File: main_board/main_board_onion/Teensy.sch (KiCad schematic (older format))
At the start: 6 parts, among them Q6 BSS138, Q7 2N7002E, U8 Teensy-LC

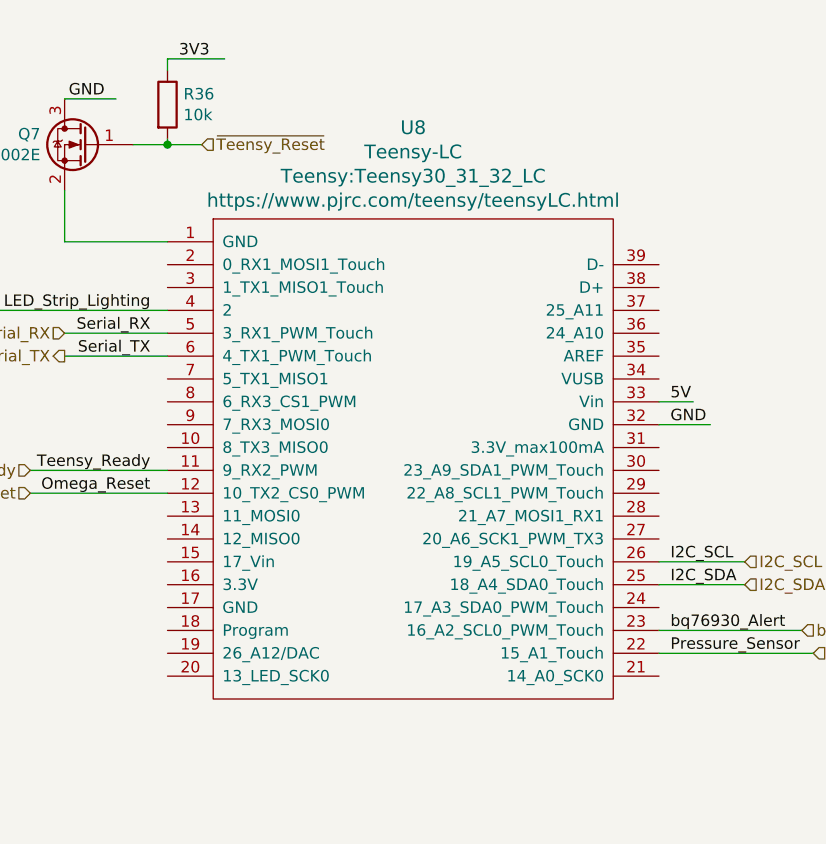
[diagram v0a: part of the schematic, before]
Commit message: Added nRF page and Adafruit Trinket files
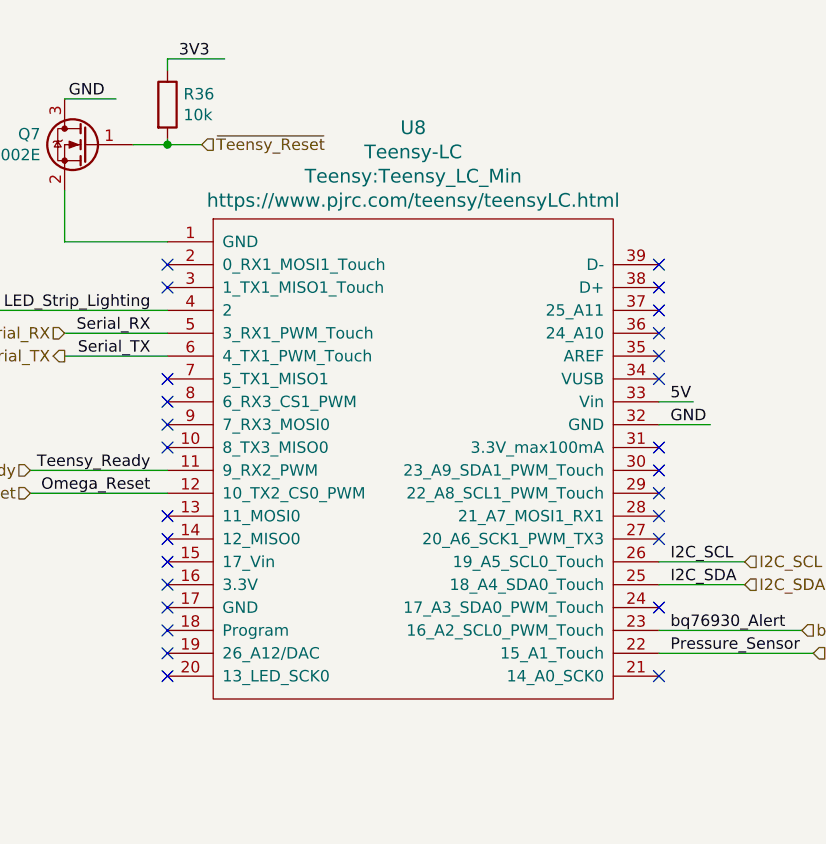
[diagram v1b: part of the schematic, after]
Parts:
- U8: footprint Teensy:Teensy30_31_32_LC -> Teensy:Teensy_LC_Min
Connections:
- no-connect marks 0 -> 27
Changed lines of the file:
@@
 $Descr A4 11693 8268
 encoding utf-8
-Sheet 5 5
+Sheet 5 6
 Title ""
 Date ""
@@
 F 0 "U8" H 5775 4874 60  0000 C CNN
 F 1 "Teensy-LC" H 5775 4768 60  0000 C CNN
-F 2 "Teensy:Teensy30_31_32_LC" H 5775 4662 60  0000 C CNN
+F 2 "Teensy:Teensy_LC_Min" H 5775 4662 60  0000 C CNN
 F 3 "https://www.pjrc.com/teensy/teensyLC.html" H 5775 4556 60  0000 C CNN
 	1    5750 3425
@@
 Text HLabel 4850 2050 2    50   Input ~ 0
 ~Teensy_Reset
+NoConn ~ 6850 2575
+NoConn ~ 6850 2675
+NoConn ~ 6850 2775
+NoConn ~ 6850 2875
+NoConn ~ 6850 2975
+NoConn ~ 6850 3075
+NoConn ~ 6850 3375
+NoConn ~ 6850 3475
+NoConn ~ 6850 3575
+NoConn ~ 6850 3675
+NoConn ~ 6850 3775
+NoConn ~ 6850 4075
+NoConn ~ 6850 4375
+NoConn ~ 4700 4375
+NoConn ~ 4700 4275
+NoConn ~ 4700 4175
+NoConn ~ 4700 4075
+NoConn ~ 4700 3975
+NoConn ~ 4700 3875
+NoConn ~ 4700 3775
+NoConn ~ 4700 3675
+NoConn ~ 4700 3375
+NoConn ~ 4700 3275
+NoConn ~ 4700 3175
+NoConn ~ 4700 3075
+NoConn ~ 4700 2675
+NoConn ~ 4700 2575
 $EndSCHEMATC

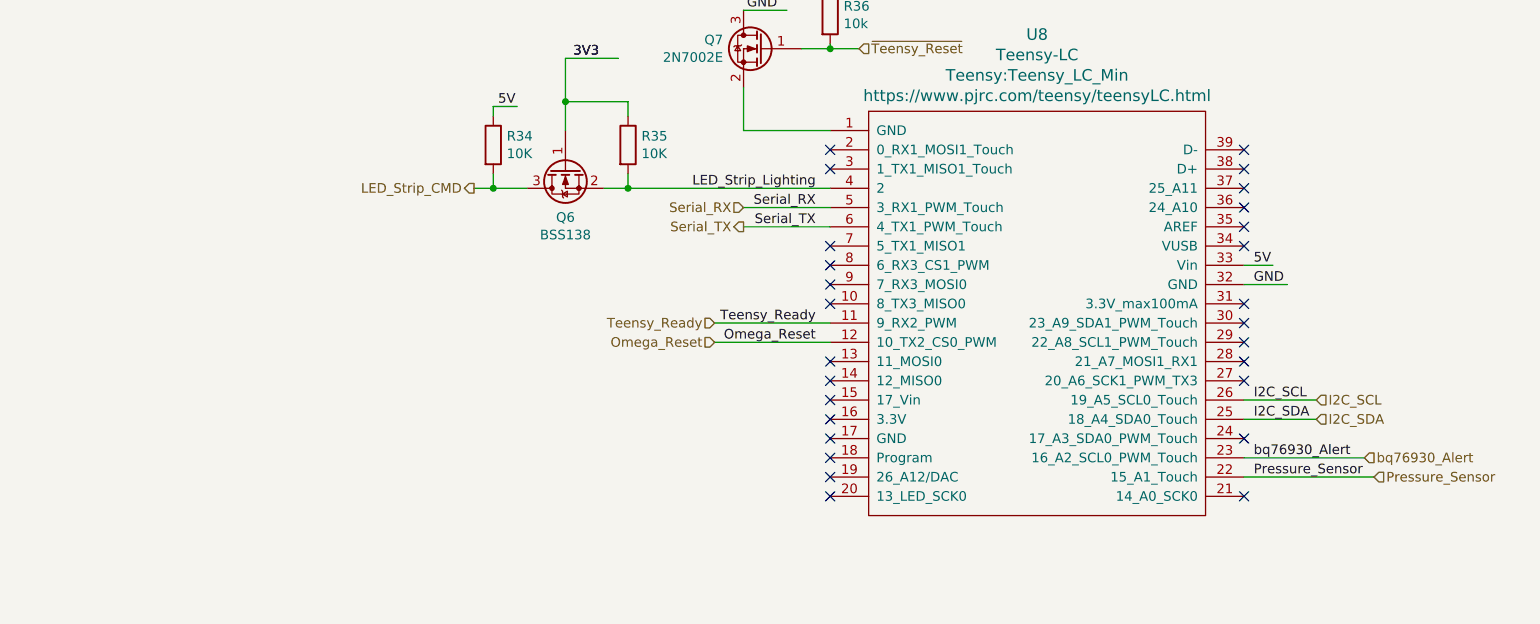
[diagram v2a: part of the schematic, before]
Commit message: Started placing Onion USB, 5v, 3v3 power.
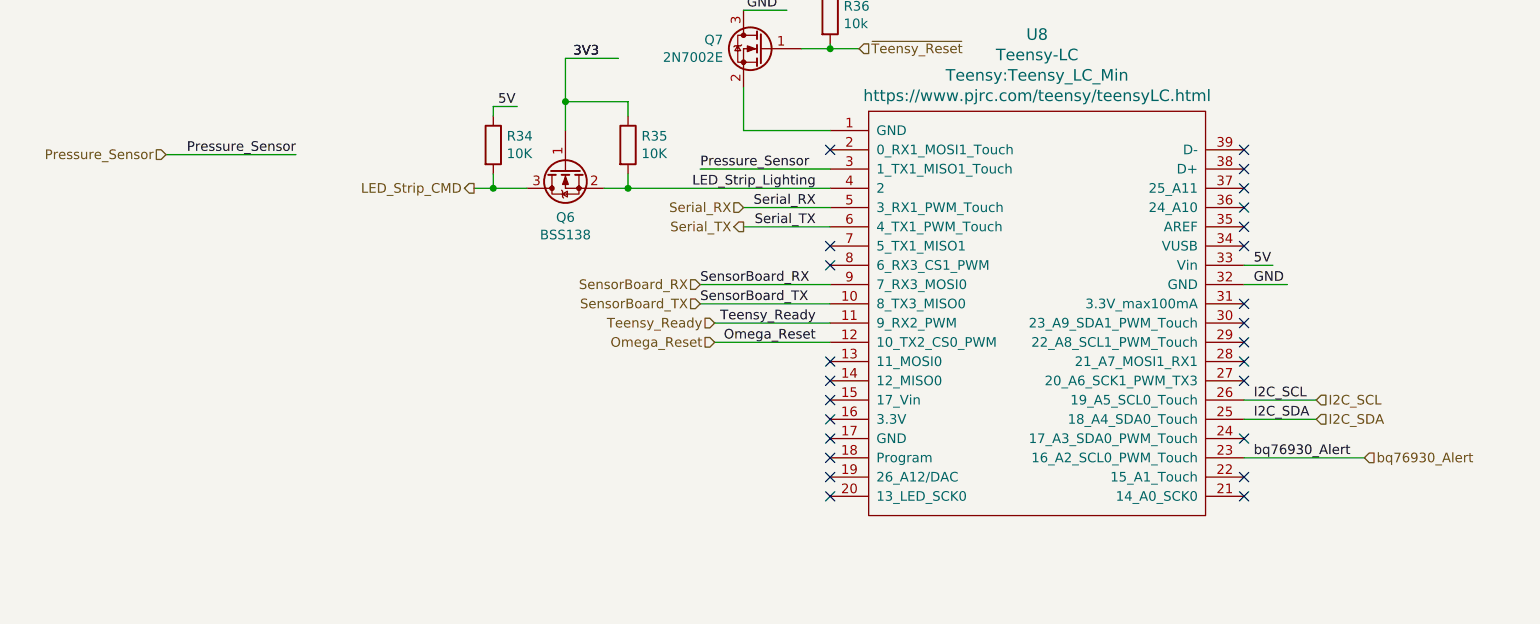
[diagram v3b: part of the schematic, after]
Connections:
- net labels added: SensorBoard_RX, SensorBoard_TX
- wire segments 34 -> 37
- no-connect marks 27 -> 25
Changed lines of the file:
@@
 Comment4 ""
 $EndDescr
-$Comp
-L Teensy:Teensy-LC U8
-U 1 1 5D055422
-P 5750 3425
-F 0 "U8" H 5775 4874 60  0000 C CNN
-F 1 "Teensy-LC" H 5775 4768 60  0000 C CNN
-F 2 "Teensy:Teensy_LC_Min" H 5775 4662 60  0000 C CNN
-F 3 "https://www.pjrc.com/teensy/teensyLC.html" H 5775 4556 60  0000 C CNN
-	1    5750 3425
-	1    0    0    -1
-$EndComp
 Text Notes 2700 7650 0    79   ~ 0
 (NOTE: Use the Pin Labels and not the actual Pin # on the Symbol)\nPins:        Function:\n2             LED Strip Lighting\n3             Serial RX1\n4             Serial TX1\n15            Analog Input (Ground Sensor)\n16            bq76930 Alert Pin             \n18            I2C SDA0\n19            I2C SCL0
@@
 Text Label 4625 2975 2    50   ~ 0
 Serial_TX
-Text Label 6900 4275 0    50   ~ 0
+Text Label 1925 2600 2    50   ~ 0
 Pressure_Sensor
 Text Label 6900 4175 0    50   ~ 0
@@
 	6850 4175 7475 4175
 Wire Wire Line
-	6850 4275 7525 4275
+	1925 2600 1250 2600
 $Comp
 L Transistor_FET:BSS138 Q6
@@
 Text HLabel 7475 4175 2    50   Input ~ 0
 bq76930_Alert
-Text HLabel 7525 4275 2    50   Input ~ 0
+Text HLabel 1250 2600 0    50   Input ~ 0
 Pressure_Sensor
 Text Label 4625 3475 2    50   ~ 0
@@
 NoConn ~ 4700 3775
 NoConn ~ 4700 3675
-NoConn ~ 4700 3375
-NoConn ~ 4700 3275
 NoConn ~ 4700 3175
 NoConn ~ 4700 3075
-NoConn ~ 4700 2675
 NoConn ~ 4700 2575
+$Comp
+L Teensy:Teensy-LC U8
+U 1 1 5D055422
+P 5750 3425
+F 0 "U8" H 5775 4874 60  0000 C CNN
+F 1 "Teensy-LC" H 5775 4768 60  0000 C CNN
+F 2 "Teensy:Teensy_LC_Min" H 5775 4662 60  0000 C CNN
+F 3 "https://www.pjrc.com/teensy/teensyLC.html" H 5775 4556 60  0000 C CNN
+	1    5750 3425
+	1    0    0    -1
+$EndComp
+Text Label 4025 3275 0    50   ~ 0
+SensorBoard_RX
+Text Label 4025 3375 0    50   ~ 0
+SensorBoard_TX
+Wire Wire Line
+	4700 3275 4025 3275
+Wire Wire Line
+	4700 3375 4025 3375
+Text HLabel 4025 3275 0    50   Input ~ 0
+SensorBoard_RX
+Text HLabel 4025 3375 0    50   Input ~ 0
+SensorBoard_TX
+Text Label 4025 2675 0    50   ~ 0
+Pressure_Sensor
+Wire Wire Line
+	4700 2675 4025 2675
+NoConn ~ 6850 4275
 $EndSCHEMATC

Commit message: Finished initial routing of this design
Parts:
- added D1: BAT42W-V, Diode_SMD:D_SOD-123, symbol Diode:BAT42W-V
- added LS1: CMT-8530S-SMT-TR, SamacSys_Parts:CMT8530SSMTTR, symbol SamacSys_Parts:CMT-8530S-SMT-TR
- added Q8: MMBT3904, Package_TO_SOT_SMD:SOT-23, symbol Transistor_BJT:MMBT3904
- added R7: 100, Resistor_SMD:R_0402_1005Metric, symbol Device:R
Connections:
- net labels added: SW_GND, buzzer
- wire segments 37 -> 50
- no-connect marks 25 -> 26
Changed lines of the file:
@@
 $Descr A4 11693 8268
 encoding utf-8
-Sheet 5 7
+Sheet 4 7
 Title ""
 Date ""
@@
 Text Label 6900 3175 0    50   ~ 0
 5V
-Text Label 6900 3275 0    50   ~ 0
-GND
 Wire Wire Line
 	6850 3175 7000 3175
-Wire Wire Line
-	6850 3275 7075 3275
 Text Label 4425 1850 2    50   ~ 0
 GND
@@
 Wire Wire Line
 	4700 1725 4700 1675
-Wire Wire Line
-	4700 1675 4950 1675
 Text Label 4750 1675 0    50   ~ 0
 3V3
@@
 NoConn ~ 4700 3775
 NoConn ~ 4700 3675
-NoConn ~ 4700 3175
 NoConn ~ 4700 3075
 NoConn ~ 4700 2575
+Text Label 4025 3275 0    50   ~ 0
+SensorBoard_RX
+Text Label 4025 3375 0    50   ~ 0
+SensorBoard_TX
+Wire Wire Line
+	4700 3275 4025 3275
+Wire Wire Line
+	4700 3375 4025 3375
+Text HLabel 4025 3275 0    50   Input ~ 0
+SensorBoard_RX
+Text HLabel 4025 3375 0    50   Input ~ 0
+SensorBoard_TX
+Text Label 4025 2675 0    50   ~ 0
+Pressure_Sensor
+Wire Wire Line
+	4700 2675 4025 2675
+NoConn ~ 6850 4275
+$Comp
+L SamacSys_Parts:CMT-8530S-SMT-TR LS1
+U 1 1 5D1128E1
+P 9675 3750
+F 0 "LS1" V 10179 3878 50  0000 L CNN
+F 1 "CMT-8530S-SMT-TR" V 10270 3878 50  0000 L CNN
+F 2 "SamacSys_Parts:CMT8530SSMTTR" H 10625 3850 50  0001 L CNN
+F 3 "https://componentsearchengine.com/Datasheets/1/CMT-8530S-SMT-TR.pdf" H 10625 3750 50  0001 L CNN
+F 4 "Speakers & Transducers Buzzer 8.5mm sq 2.73kHz 3.6V SMT" H 10625 3650 50  0001 L CNN "Description"
+F 5 "3" H 10625 3550 50  0001 L CNN "Height"
+F 6 "490-CMT-8530S-SMT-TR" H 10625 3450 50  0001 L CNN "Mouser Part Number"
+F 7 "https://www.mouser.com/Search/Refine.aspx?Keyword=490-CMT-8530S-SMT-TR" H 10625 3350 50  0001 L CNN "Mouser Price/Stock"
+F 8 "CUI" H 10625 3250 50  0001 L CNN "Manufacturer_Name"
+F 9 "CMT-8530S-SMT-TR" H 10625 3150 50  0001 L CNN "Manufacturer_Part_Number"
+	1    9675 3750
+	0    1    1    0
+$EndComp
+Wire Wire Line
+	4700 1675 4950 1675
+Text Label 9725 3625 2    50   ~ 0
+3V3
+NoConn ~ 9675 3750
+NoConn ~ 9575 4850
+Wire Wire Line
+	9575 3750 9575 3625
+Wire Wire Line
+	9575 3625 9725 3625
+$Comp
+L Diode:BAT42W-V D1
+U 1 1 5D11BE45
+P 9000 4300
+F 0 "D1" V 8954 4379 50  0000 L CNN
+F 1 "BAT42W-V" V 9045 4379 50  0000 L CNN
+F 2 "Diode_SMD:D_SOD-123" H 9000 4125 50  0001 C CNN
+F 3 "http://www.vishay.com/docs/85660/bat42.pdf" H 9000 4300 50  0001 C CNN
+	1    9000 4300
+	0    1    1    0
+$EndComp
+Wire Wire Line
+	9575 3750 9000 3750
+Wire Wire Line
+	9000 3750 9000 4150
+Connection ~ 9575 3750
+$Comp
+L Transistor_BJT:MMBT3904 Q8
+U 1 1 5D11DB7A
+P 9575 5225
+F 0 "Q8" H 9766 5271 50  0000 L CNN
+F 1 "MMBT3904" H 9766 5180 50  0000 L CNN
+F 2 "Package_TO_SOT_SMD:SOT-23" H 9775 5150 50  0001 L CIN
+F 3 "https://www.fairchildsemi.com/datasheets/2N/2N3904.pdf" H 9575 5225 50  0001 L CNN
+	1    9575 5225
+	1    0    0    -1
+$EndComp
+$Comp
+L Device:R R7
+U 1 1 5D11E980
+P 9125 5225
+F 0 "R7" V 8918 5225 50  0000 C CNN
+F 1 "100" V 9009 5225 50  0000 C CNN
+F 2 "Resistor_SMD:R_0402_1005Metric" V 9055 5225 50  0001 C CNN
+F 3 "~" H 9125 5225 50  0001 C CNN
+	1    9125 5225
+	0    1    1    0
+$EndComp
+Wire Wire Line
+	9275 5225 9375 5225
+Text Label 9475 5500 0    50   ~ 0
+GND
+Wire Wire Line
+	9675 5425 9675 5500
+Wire Wire Line
+	9675 5500 9475 5500
+Text Label 8700 5225 0    50   ~ 0
+buzzer
+Wire Wire Line
+	8975 5225 8700 5225
 $Comp
 L Teensy:Teensy-LC U8
@@
 	1    0    0    -1
 $EndComp
-Text Label 4025 3275 0    50   ~ 0
-SensorBoard_RX
-Text Label 4025 3375 0    50   ~ 0
-SensorBoard_TX
-Wire Wire Line
-	4700 3275 4025 3275
-Wire Wire Line
-	4700 3375 4025 3375
-Text HLabel 4025 3275 0    50   Input ~ 0
-SensorBoard_RX
-Text HLabel 4025 3375 0    50   Input ~ 0
-SensorBoard_TX
-Text Label 4025 2675 0    50   ~ 0
-Pressure_Sensor
-Wire Wire Line
-	4700 2675 4025 2675
-NoConn ~ 6850 4275
+Text Label 4425 3175 0    50   ~ 0
+buzzer
+Wire Wire Line
+	4700 3175 4425 3175
+Wire Wire Line
+	9675 4850 9675 4900
+Wire Wire Line
+	9000 4450 9000 4900
+Wire Wire Line
+	9000 4900 9675 4900
+Connection ~ 9675 4900
+Wire Wire Line
+	9675 4900 9675 5025
+Text Label 4600 2475 2    50   ~ 0
+SW_GND
+Text Label 7200 3275 2    50   ~ 0
+SW_GND
+Wire Wire Line
+	6850 3275 7200 3275
 $EndSCHEMATC

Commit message: went back to original Macrofab v2 files and made changes for v3.5
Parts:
- removed Q7: 2N7002E, Package_TO_SOT_SMD:SOT-23, symbol Transistor_FET:2N7002E
- removed R36: 10k, Resistor_SMD:R_0603_1608Metric, symbol Device:R
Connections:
- net labels added: Teensy_Program
- net labels removed: Omega_Reset, SW_GND
- wire segments 50 -> 44
- no-connect marks 26 -> 25
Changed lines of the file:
@@
-EESchema Schematic File Version 5
+EESchema Schematic File Version 4
 LIBS:main_board_onion-cache
-EELAYER 29 0
+EELAYER 30 0
 EELAYER END
 $Descr A4 11693 8268
@@
 Wire Wire Line
 	6850 3175 7000 3175
-Text Label 4425 1850 2    50   ~ 0
+Text Label 4625 2475 2    50   ~ 0
 GND
 Text Label 4625 2775 2    50   ~ 0
 LED_Strip_Lighting
-Text Label 4625 2875 2    50   ~ 0
+Text Label 4625 2575 2    50   ~ 0
 Serial_RX
-Text Label 4625 2975 2    50   ~ 0
+Text Label 4625 2675 2    50   ~ 0
 Serial_TX
 Text Label 1925 2600 2    50   ~ 0
@@
 I2C_SCL
 Wire Wire Line
-	4700 2875 4250 2875
-Wire Wire Line
-	4700 2975 4250 2975
+	4700 2575 4250 2575
+Wire Wire Line
+	4700 2675 4250 2675
 Wire Wire Line
 	6850 3875 7225 3875
@@
 U 1 1 5D01CEE1
 P 3650 2550
-F 0 "R35" H 3720 2596 50  0000 L CNN
-F 1 "10K" H 3720 2505 50  0000 L CNN
+F 0 "R35" H 3450 2600 50  0000 L CNN
+F 1 "10K" H 3450 2475 50  0000 L CNN
 F 2 "Resistor_SMD:R_0603_1608Metric" V 3580 2550 50  0001 C CNN
 F 3 "~" H 3650 2550 50  0001 C CNN
@@
 Text HLabel 2850 2775 0    50   Output ~ 0
 LED_Strip_CMD
-Text HLabel 4250 2875 0    50   Input ~ 0
+Text HLabel 4250 2575 0    50   Input ~ 0
 Serial_RX
-Text HLabel 4250 2975 0    50   Output ~ 0
+Text HLabel 4250 2675 0    50   Output ~ 0
 Serial_TX
 Text HLabel 7225 3875 2    50   Input ~ 0
@@
 Text HLabel 4100 3475 0    50   Input ~ 0
 Teensy_Ready
-Text Label 4625 3575 2    50   ~ 0
-Omega_Reset
-Wire Wire Line
-	4700 3575 4100 3575
-Text HLabel 4100 3575 0    50   Input ~ 0
-Omega_Reset
-Wire Wire Line
-	4700 2475 4250 2475
-Wire Wire Line
-	4250 2475 4250 2250
-$Comp
-L Transistor_FET:2N7002E Q7
-U 1 1 5D099095
-P 4350 2050
-F 0 "Q7" H 4556 2096 50  0000 L CNN
-F 1 "2N7002E" H 4556 2005 50  0000 L CNN
-F 2 "Package_TO_SOT_SMD:SOT-23" H 4550 1975 50  0001 L CIN
-F 3 "http://www.diodes.com/assets/Datasheets/ds30376.pdf" H 4350 2050 50  0001 L CNN
-	1    4350 2050
-	-1   0    0    -1
-$EndComp
-Wire Wire Line
-	4475 1850 4250 1850
-$Comp
-L Device:R R36
-U 1 1 5D0AE8F9
-P 4700 1875
-F 0 "R36" H 4770 1921 50  0000 L CNN
-F 1 "10k" H 4770 1830 50  0000 L CNN
-F 2 "Resistor_SMD:R_0603_1608Metric" V 4630 1875 50  0001 C CNN
-F 3 "~" H 4700 1875 50  0001 C CNN
-	1    4700 1875
-	1    0    0    -1
-$EndComp
-Wire Wire Line
-	4550 2050 4700 2050
-Wire Wire Line
-	4700 2050 4700 2025
-Connection ~ 4700 2050
-Wire Wire Line
-	4700 2050 4850 2050
-Wire Wire Line
-	4700 1725 4700 1675
-Text Label 4750 1675 0    50   ~ 0
-3V3
 Text Label 3500 2100 2    50   ~ 0
 3V3
-Text HLabel 4850 2050 2    50   Input ~ 0
-~Teensy_Reset
 NoConn ~ 6850 2575
 NoConn ~ 6850 2675
@@
 NoConn ~ 6850 4375
 NoConn ~ 4700 4375
-NoConn ~ 4700 4275
-NoConn ~ 4700 4175
 NoConn ~ 4700 4075
 NoConn ~ 4700 3975
@@
 NoConn ~ 4700 3675
 NoConn ~ 4700 3075
-NoConn ~ 4700 2575
 Text Label 4025 3275 0    50   ~ 0
 SensorBoard_RX
@@
 Text HLabel 4025 3375 0    50   Input ~ 0
 SensorBoard_TX
-Text Label 4025 2675 0    50   ~ 0
+Text Label 4025 2875 0    50   ~ 0
 Pressure_Sensor
 Wire Wire Line
-	4700 2675 4025 2675
+	4700 2875 4025 2875
 NoConn ~ 6850 4275
 $Comp
@@
 	0    1    1    0
 $EndComp
-Wire Wire Line
-	4700 1675 4950 1675
 Text Label 9725 3625 2    50   ~ 0
 3V3
@@
 Wire Wire Line
 	9675 4900 9675 5025
-Text Label 4600 2475 2    50   ~ 0
-SW_GND
-Text Label 7200 3275 2    50   ~ 0
-SW_GND
 Wire Wire Line
 	6850 3275 7200 3275
+Wire Wire Line
+	4700 2475 4450 2475
+NoConn ~ 4700 2975
+Text HLabel 4550 4275 0    50   Input ~ 0
+~Teensy_Reset
+Wire Wire Line
+	4700 4275 4550 4275
+Text Label 7050 3275 2    50   ~ 0
+GND
+Text HLabel 4550 4175 0    50   Input ~ 0
+Teensy_Program
+Wire Wire Line
+	4700 4175 4550 4175
+NoConn ~ 4700 3575
 $EndSCHEMATC
